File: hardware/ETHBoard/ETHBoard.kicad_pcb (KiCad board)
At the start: 2 copper layers, 25.1 x 12.2 mm, 28 parts, among them J1 Conn_02x04_Odd_Even, J2 Conn_01x02_Pin, U1 LAN8651B1-E_LMX, Y1 X322525MOB4SI

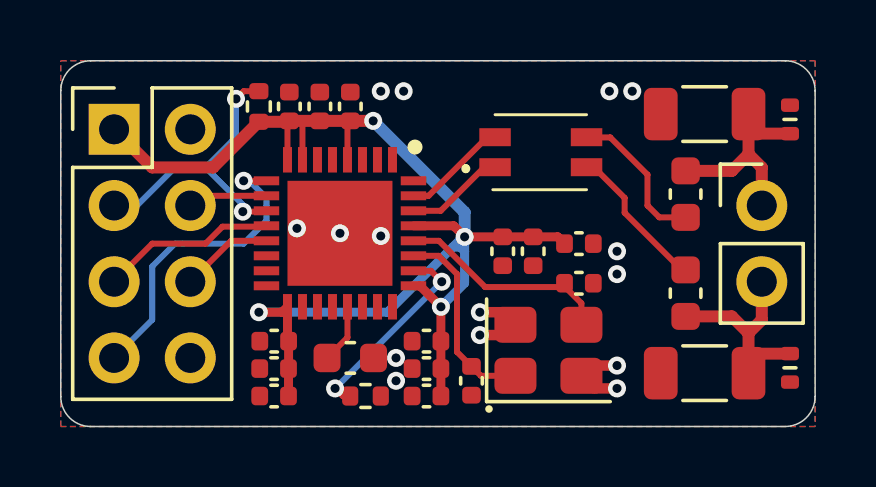
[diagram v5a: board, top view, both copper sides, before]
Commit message: Added termination parts for ETHBoard.
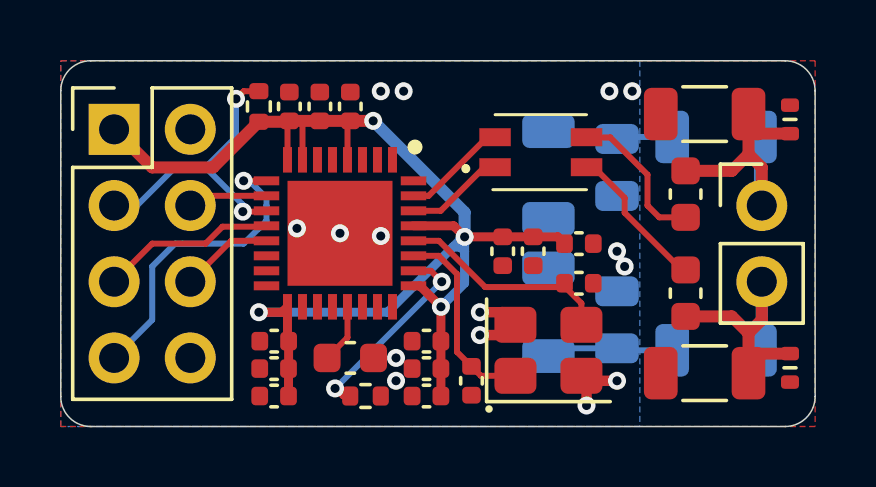
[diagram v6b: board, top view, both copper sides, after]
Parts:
- added C18: 220nF, Capacitor_SMD:C_0805_2012Metric, B.Cu at (92.2, 59.4)
- added C19: 220nF, Capacitor_SMD:C_0805_2012Metric, B.Cu at (92.2, 54.4)
- added R5: 49.9Ω, Resistor_SMD:R_1206_3216Metric, B.Cu at (95.5, 60.5)
- added R6: 49.9Ω, Resistor_SMD:R_1206_3216Metric, B.Cu at (95.5, 53.3)
- added R7: 100kΩ, Resistor_SMD:R_1206_3216Metric, B.Cu at (89.9, 54.6)
- added R8: 100kΩ, Resistor_SMD:R_1206_3216Metric, B.Cu at (89.9, 59.2)
- renumbered R5 to R3, R6 to R4
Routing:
- net Net-(C19-Pad2): track 0.00 -> 4.26 mm
- net Net-(C18-Pad2): track 0.00 -> 4.26 mm
- net /T1S_d+: track 7.75 -> 10.1 mm
- net /T1S_d-: track 7.59 -> 9.90 mm
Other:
- board text added: "COMChallenge ETH TRCV v1.0 github.com/ raphweb"
- board text removed: "COMChallenge ETH TRCV v1.0 github.com/raphweb"

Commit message: Larger resistors and more GND vias.
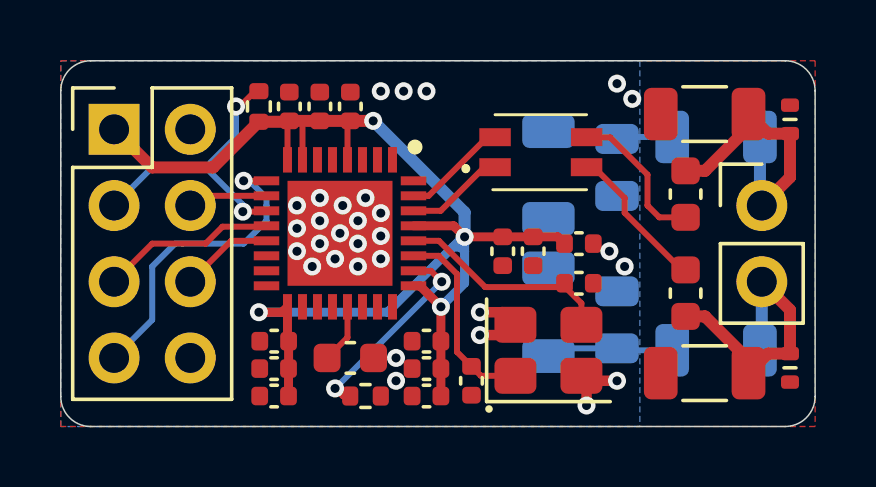
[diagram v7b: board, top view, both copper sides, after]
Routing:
- net GND: vias 15 -> 30
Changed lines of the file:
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@@
 		(sheetfile "ETHBoard.kicad_sch")
 		(clearance 0.15)
-		(attr smd exclude_from_pos_files exclude_from_bom)
+		(attr smd exclude_from_pos_files)
 		(fp_circle
 			(center -2.875 -2.5)
@@
 			)
 		)
-		(property "LCSC" "C5378"
+		(property "LCSC" "C307331"
 			(at 0 0 270)
 			(unlocked yes)
@@
 			)
 		)
-		(property "LCSC" "C17900"
+		(property "LCSC" "C17902"
 			(at 0 0 270)
 			(unlocked yes)
@@
 			)
 		)
-		(property "LCSC" "C18018"
+		(property "LCSC" "C17902"
 			(at 0 0 180)
 			(unlocked yes)
@@
 			)
 		)
-		(property "LCSC" "C5378"
+		(property "LCSC" "C307331"
 			(at 0 0 90)
 			(unlocked yes)
@@
 			)
 		)
-		(property "LCSC" "C17900"
+		(property "LCSC" "C17902"
 			(at 0 0 270)
 			(unlocked yes)
@@
 			)
 		)
-		(property "LCSC" "C18018"
+		(property "LCSC" "C17902"
 			(at 0 0 0)
 			(unlocked yes)
@@
 	)
 	(via
-		(at 92.202 57.15)
+		(at 84.328 57.404)
+		(size 0.6)
+		(drill 0.3)
+		(layers "F.Cu" "B.Cu")
+		(free yes)
+		(net 2)
+	)
+	(via
+		(at 91.948 57.15)
+		(size 0.6)
+		(drill 0.3)
+		(layers "F.Cu" "B.Cu")
+		(free yes)
+		(net 2)
+	)
+	(via
+		(at 83.566 56.134)
+		(size 0.6)
+		(drill 0.3)
+		(layers "F.Cu" "B.Cu")
+		(free yes)
+		(net 2)
+	)
+	(via
+		(at 82.296 55.372)
+		(size 0.6)
+		(drill 0.3)
+		(layers "F.Cu" "B.Cu")
+		(free yes)
+		(net 2)
+	)
+	(via
+		(at 83.566 57.658)
+		(size 0.6)
+		(drill 0.3)
+		(layers "F.Cu" "B.Cu")
+		(free yes)
+		(net 2)
+	)
+	(via
+		(at 83.058 55.626)
+		(size 0.6)
+		(drill 0.3)
+		(layers "F.Cu" "B.Cu")
+		(free yes)
+		(net 2)
+	)
+	(via
+		(at 92.71 52.07)
+		(size 0.6)
+		(drill 0.3)
+		(layers "F.Cu" "B.Cu")
+		(free yes)
+		(net 2)
+	)
+	(via
+		(at 83.82 55.372)
+		(size 0.6)
+		(drill 0.3)
+		(layers "F.Cu" "B.Cu")
+		(free yes)
+		(net 2)
+	)
+	(via
+		(at 81.534 57.15)
 		(size 0.6)
 		(drill 0.3)
@@
 	)
 	(via
-		(at 92.71 51.816)
+		(at 82.296 56.896)
 		(size 0.6)
 		(drill 0.3)
@@
 	)
 	(via
-		(at 91.948 51.816)
+		(at 92.202 51.562)
+		(size 0.6)
+		(drill 0.3)
+		(layers "F.Cu" "B.Cu")
+		(free yes)
+		(net 2)
+	)
+	(via
+		(at 81.534 55.626)
 		(size 0.6)
 		(drill 0.3)
@@
 	)
 	(via
+		(at 82.042 57.658)
+		(size 0.6)
+		(drill 0.3)
+		(layers "F.Cu" "B.Cu")
+		(free yes)
+		(net 2)
+	)
+	(via
+		(at 82.804 57.404)
+		(size 0.6)
+		(drill 0.3)
+		(layers "F.Cu" "B.Cu")
+		(free yes)
+		(net 2)
+	)
+	(via
+		(at 83.566 56.896)
+		(size 0.6)
+		(drill 0.3)
+		(layers "F.Cu" "B.Cu")
+		(free yes)
+		(net 2)
+	)
+	(via
 		(at 84.328 56.642)
 		(size 0.6)
@@
 	)
 	(via
+		(at 85.852 51.816)
+		(size 0.6)
+		(drill 0.3)
+		(layers "F.Cu" "B.Cu")
+		(free yes)
+		(net 2)
+	)
+	(via
+		(at 82.296 56.134)
+		(size 0.6)
+		(drill 0.3)
+		(layers "F.Cu" "B.Cu")
+		(free yes)
+		(net 2)
+	)
+	(via
 		(at 82.968 56.552)
 		(size 0.6)
@@
 	)
 	(via
+		(at 84.328 55.88)
+		(size 0.6)
+		(drill 0.3)
+		(layers "F.Cu" "B.Cu")
+		(free yes)
+		(net 2)
+	)
+	(via
 		(at 87.63 59.182)
 		(size 0.6)
@@
 	)
 	(segment
-		(start 96.5855 52.578)
-		(end 96.5855 53.228)
+		(start 94.488 54.47)
+		(end 95.136 54.47)
 		(width 0.4)
 		(layer "F.Cu")
@@
 	)
 	(segment
-		(start 94.488 54.47)
-		(end 96.029 54.47)
+		(start 97.9678 53.2308)
+		(end 97.9678 54.6862)
 		(width 0.4)
 		(layer "F.Cu")
@@
 	)
 	(segment
-		(start 97.028 54.356)
-		(end 97.028 55.626)
+		(start 97.9678 53.2308)
+		(end 97.2383 53.2308)
 		(width 0.4)
 		(layer "F.Cu")
@@
 	)
 	(segment
-		(start 96.5855 52.578)
-		(end 96.5855 53.9135)
+		(start 96.5855 53.0205)
+		(end 96.5855 52.578)
 		(width 0.4)
 		(layer "F.Cu")
@@
 	)
 	(segment
-		(start 96.029 54.47)
-		(end 96.5855 53.9135)
+		(start 97.9678 54.6862)
+		(end 97.028 55.626)
 		(width 0.4)
 		(layer "F.Cu")
@@
 	)
 	(segment
-		(start 96.5855 53.228)
-		(end 97.9678 53.228)
+		(start 95.136 54.47)
+		(end 96.5855 53.0205)
 		(width 0.4)
 		(layer "F.Cu")
@@
 	)
 	(segment
-		(start 96.5855 53.9135)
-		(end 97.028 54.356)
+		(start 97.2383 53.2308)
+		(end 96.5855 52.578)
 		(width 0.4)
 		(layer "F.Cu")
@@
 	)
 	(segment
-		(start 97.9678 60.564)
-		(end 96.6975 60.564)
+		(start 97.9678 60.5612)
+		(end 97.9678 59.1058)
 		(width 0.4)
 		(layer "F.Cu")
@@
 	(segment
 		(start 94.488 59.322)
-		(end 96.029 59.322)
-		(width 0.4)
-		(layer "F.Cu")
-		(net 7)
-	)
-	(segment
-		(start 96.5855 61.214)
-		(end 96.5855 59.8785)
+		(end 95.136 59.322)
 		(width 0.4)
 		(layer "F.Cu")
@@
 	)
 	(segment
-		(start 96.5855 60.452)
+		(start 96.5855 60.7715)
 		(end 96.5855 61.214)
 		(width 0.4)
@@
 	)
 	(segment
-		(start 96.6975 60.564)
-		(end 96.5855 60.452)
+		(start 97.2383 60.5612)
+		(end 97.9678 60.5612)
 		(width 0.4)
 		(layer "F.Cu")
@@
 	)
 	(segment
-		(start 96.5855 59.8785)
-		(end 97.028 59.436)
+		(start 96.5855 61.214)
+		(end 97.2383 60.5612)
 		(width 0.4)
 		(layer "F.Cu")
@@
 	)
 	(segment
-		(start 96.029 59.322)
-		(end 96.5855 59.8785)
+		(start 95.136 59.322)
+		(end 96.5855 60.7715)
 		(width 0.4)
 		(layer "F.Cu")
@@
 	)
 	(segment
-		(start 97.028 59.436)
+		(start 97.9678 59.1058)
 		(end 97.028 58.166)
 		(width 0.4)
@@
 	)
 	(segment
-		(start 80.262 51.816)
-		(end 80.264 51.814)
+		(start 79.729039 55.829647)
+		(end 80.490353 55.829647)
 		(width 0.2)
 		(layer "F.Cu")
@@
 	)
 	(segment
-		(start 79.729039 55.829647)
-		(end 80.490353 55.829647)
+		(start 80.139 51.814)
+		(end 80.264 51.814)
 		(width 0.2)
 		(layer "F.Cu")
@@
 	)
 	(segment
-		(start 79.756 51.816)
-		(end 80.262 51.816)
+		(start 79.629 52.324)
+		(end 80.139 51.814)
 		(width 0.2)
 		(layer "F.Cu")
@@
 	)
 	(segment
-		(start 79.502 52.07)
-		(end 79.756 51.816)
+		(start 80.490353 55.829647)
+		(end 80.518 55.802)
 		(width 0.2)
 		(layer "F.Cu")
@@
 	)
 	(segment
-		(start 80.490353 55.829647)
-		(end 80.518 55.802)
+		(start 79.502 52.324)
+		(end 79.629 52.324)
 		(width 0.2)
 		(layer "F.Cu")
@@
 	)
 	(via
-		(at 79.502 52.07)
+		(at 79.502 52.324)
 		(size 0.6)
 		(drill 0.3)
@@
 	)
 	(segment
-		(start 79.502 53.34)
-		(end 78.486 54.356)
-		(width 0.2)
-		(layer "B.Cu")
-		(net 8)
-	)
-	(segment
-		(start 77.47 54.356)
+		(start 76.708 54.356)
 		(end 78.486 54.356)
 		(width 0.2)
@@
 	(segment
 		(start 75.438 55.626)
-		(end 76.2 55.626)
+		(end 76.708 54.356)
 		(width 0.2)
 		(layer "B.Cu")
@@
 	)
 	(segment
-		(start 76.2 55.626)
-		(end 77.47 54.356)
+		(start 79.502 53.34)
+		(end 78.486 54.356)
 		(width 0.2)
 		(layer "B.Cu")
@@
 	)
 	(segment
-		(start 79.502 52.07)
+		(start 79.502 52.324)
 		(end 79.502 53.34)
 		(width 0.2)
@@
 		(polygon
 			(pts
-				(xy 93.515951 53.933935) (xy 91.566324 52.072684) (xy 91.566324 55.323884) (xy 93.515951 57.185135)
+				(xy 93.515951 53.425935) (xy 91.566324 51.564684) (xy 91.566324 55.323884) (xy 93.515951 57.185135)
 			)
 		)
@@
 		(polygon
 			(pts
-				(xy 93.897759 57.51602) (xy 92.018159 55.61102) (xy 92.018159 56.53) (xy 93.897759 58.45582)
+				(xy 93.897759 57.51602) (xy 91.510159 55.10302) (xy 91.510159 56.388) (xy 91.694 56.388) (xy 93.897759 58.674)
 			)
 		)
@@
 		(polygon
 			(pts
-				(xy 85.728357 54.095549) (xy 87.760357 52.063549) (xy 87.760357 55.365549) (xy 85.728357 57.397549)
+				(xy 85.728357 53.587549) (xy 87.760357 51.555549) (xy 87.757 56.134) (xy 85.728357 57.397549)
 			)
 		)
@@
 		(polygon
 			(pts
-				(xy 87.757 52.07) (xy 91.567 52.07) (xy 91.567 55.626) (xy 87.757 55.626)
+				(xy 87.757 51.562) (xy 91.567 51.562) (xy 91.567 56.388) (xy 87.757 56.388)
 			)
 		)

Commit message: Updated step files for all boards, footprints for LINBoard.
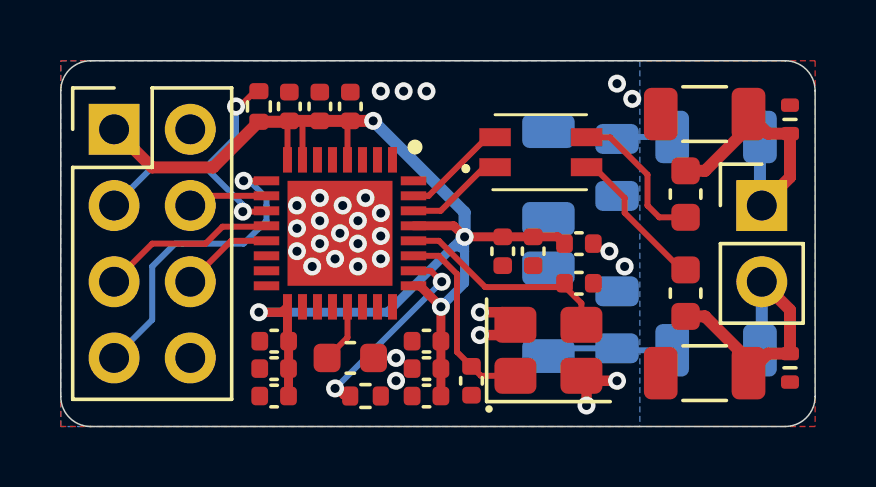
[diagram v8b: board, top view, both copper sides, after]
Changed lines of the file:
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@@
 		(sheetname "/")
 		(sheetfile "ETHBoard.kicad_sch")
-		(clearance 0.15)
 		(attr smd exclude_from_pos_files)
 		(fp_circle
@@
 			(layer "F.Fab")
 		)
+		(fp_text user "${REFERENCE}"
+			(at 0 0 0)
+			(layer "F.Fab")
+			(effects
+				(font
+					(size 0.8 0.8)
+					(thickness 0.12)
+				)
+			)
+		)
 		(pad "1" smd roundrect
 			(at -1.1 0.85)
@@
 			)
 			(rotate
-				(xyz -90 0 0)
+				(xyz 0 0 0)
 			)
 		)
@@
 			(layer "F.Fab")
 		)
-		(pad "1" thru_hole oval
+		(pad "1" thru_hole rect
 			(at 0 0)
 			(size 1.7 1.7)
@@
 			(layer "B.Fab")
 		)
+		(fp_text user "${REFERENCE}"
+			(at 0 0 270)
+			(layer "B.Fab")
+			(effects
+				(font
+					(size 0.5 0.5)
+					(thickness 0.08)
+				)
+				(justify mirror)
+			)
+		)
 		(pad "1" smd roundrect
 			(at -0.95 0 90)
@@
 			(layer "B.Fab")
 		)
+		(fp_text user "${REFERENCE}"
+			(at 0 0 270)
+			(layer "B.Fab")
+			(effects
+				(font
+					(size 0.8 0.8)
+					(thickness 0.12)
+				)
+				(justify mirror)
+			)
+		)
 		(pad "1" smd roundrect
 			(at -1.4625 0 90)
@@
 			(layer "B.Fab")
 		)
+		(fp_text user "${REFERENCE}"
+			(at 0 0 180)
+			(layer "B.Fab")
+			(effects
+				(font
+					(size 0.8 0.8)
+					(thickness 0.12)
+				)
+				(justify mirror)
+			)
+		)
 		(pad "1" smd roundrect
 			(at -1.4625 0)
@@
 			(layer "B.Fab")
 		)
+		(fp_text user "${REFERENCE}"
+			(at 0 0 90)
+			(layer "B.Fab")
+			(effects
+				(font
+					(size 0.5 0.5)
+					(thickness 0.08)
+				)
+				(justify mirror)
+			)
+		)
 		(pad "1" smd roundrect
 			(at -0.95 0 270)
@@
 			(layer "B.Fab")
 		)
+		(fp_text user "${REFERENCE}"
+			(at 0 0 270)
+			(layer "B.Fab")
+			(effects
+				(font
+					(size 0.8 0.8)
+					(thickness 0.12)
+				)
+				(justify mirror)
+			)
+		)
 		(pad "1" smd roundrect
 			(at -1.4625 0 90)
@@
 			(layer "B.Fab")
 		)
+		(fp_text user "${REFERENCE}"
+			(at 0 0 0)
+			(layer "B.Fab")
+			(effects
+				(font
+					(size 0.8 0.8)
+					(thickness 0.12)
+				)
+				(justify mirror)
+			)
+		)
 		(pad "1" smd roundrect
